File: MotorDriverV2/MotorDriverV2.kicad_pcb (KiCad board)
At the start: 2 copper layers, 9 parts, among them IC1 TC78H620FNG, IC2 ESP32-C3FH4X, J1 Power, J2 Input, J3 Out_A, J4 Out_B

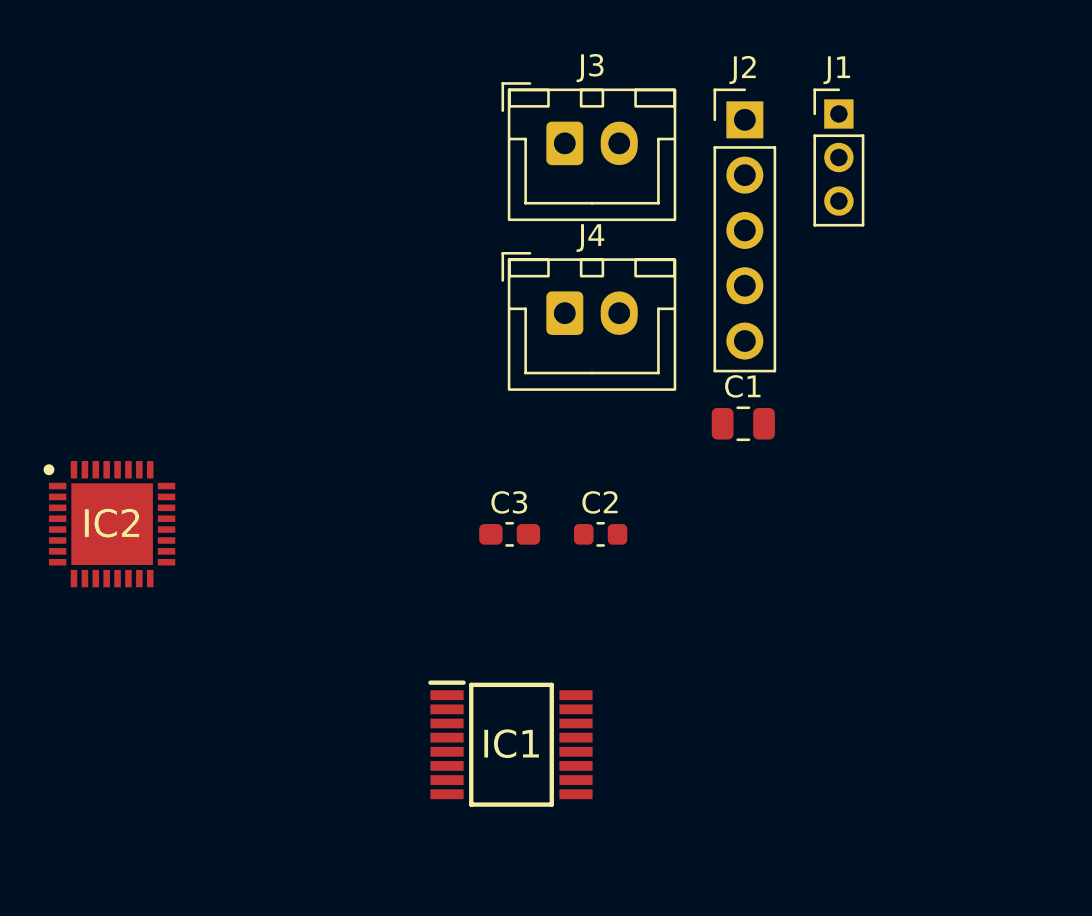
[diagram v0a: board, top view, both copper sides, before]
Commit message: UPDATE: Added symbols, fotprints and datasheets for components
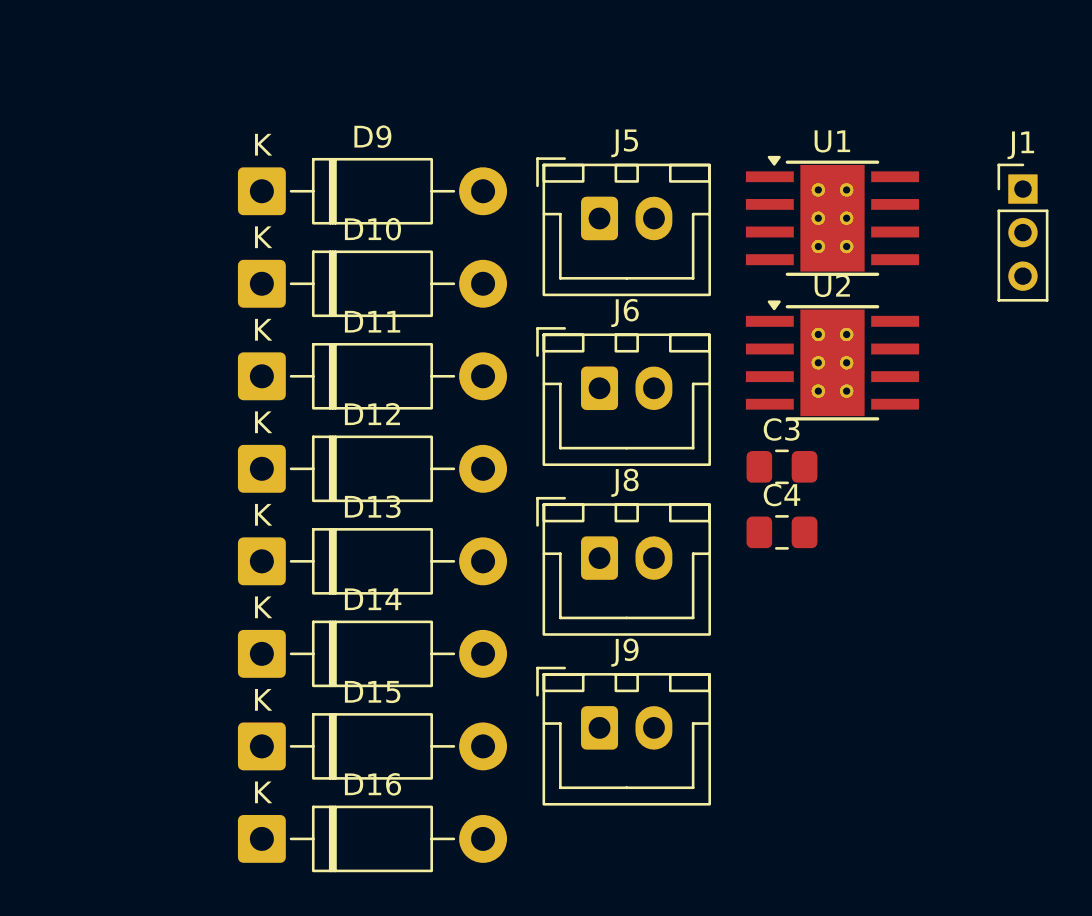
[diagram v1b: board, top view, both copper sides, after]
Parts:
- removed C1: 100uF, Capacitor_SMD:C_0805_2012Metric
- removed C2: C, Capacitor_SMD:C_0603_1608Metric
- removed IC1: TC78H620FNG, TC78H620FNG:SOP65P640X160-16N
- removed IC2: ESP32-C3FH4X, ESP32-C3FH4X:QFN50P500X500X90-33N-D
- removed J2: Input, Connector_PinHeader_2.54mm:PinHeader_1x05_P2.54mm_Vertical
- removed J3: Out_A, Connector_JST:JST_XH_B2B-XH-A_1x02_P2.50mm_Vertical
- removed J4: Out_B, Connector_JST:JST_XH_B2B-XH-A_1x02_P2.50mm_Vertical
- added C4: 100uF, Capacitor_SMD:C_0805_2012Metric_Pad1.18x1.45mm_HandSolder, F.Cu at (137.7, 82.5)
- added D10: 1N4001, Diode_THT:D_DO-41_SOD81_P10.16mm_Horizontal, F.Cu at (113.8, 71.0)
- added D11: 1N4001, Diode_THT:D_DO-41_SOD81_P10.16mm_Horizontal, F.Cu at (113.8, 75.3)
- added D12: 1N4001, Diode_THT:D_DO-41_SOD81_P10.16mm_Horizontal, F.Cu at (113.8, 79.5)
- added D13: 1N4001, Diode_THT:D_DO-41_SOD81_P10.16mm_Horizontal, F.Cu at (113.8, 83.8)
- added D14: 1N4001, Diode_THT:D_DO-41_SOD81_P10.16mm_Horizontal, F.Cu at (113.8, 88.0)
- added D15: 1N4001, Diode_THT:D_DO-41_SOD81_P10.16mm_Horizontal, F.Cu at (113.8, 92.3)
- added D16: 1N4001, Diode_THT:D_DO-41_SOD81_P10.16mm_Horizontal, F.Cu at (113.8, 96.5)
- added D9: 1N4001, Diode_THT:D_DO-41_SOD81_P10.16mm_Horizontal, F.Cu at (113.8, 66.8)
- added J5: Out_A, Connector_JST:JST_XH_B2B-XH-A_1x02_P2.50mm_Vertical, F.Cu at (129.4, 68.0)
- added J6: Out_B, Connector_JST:JST_XH_B2B-XH-A_1x02_P2.50mm_Vertical, F.Cu at (129.4, 75.8)
- added J8: Out_A, Connector_JST:JST_XH_B2B-XH-A_1x02_P2.50mm_Vertical, F.Cu at (129.4, 83.6)
- added J9: Out_B, Connector_JST:JST_XH_B2B-XH-A_1x02_P2.50mm_Vertical, F.Cu at (129.4, 91.4)
- added U1: DRV8871DDA, Package_SO:Texas_HTSOP-8-1EP_3.9x4.9mm_P1.27mm_EP2.95x4.9mm_Mask2.4x3.1mm_ThermalVias, F.Cu at (140.1, 68.0)
- added U2: DRV8871DDA, Package_SO:Texas_HTSOP-8-1EP_3.9x4.9mm_P1.27mm_EP2.95x4.9mm_Mask2.4x3.1mm_ThermalVias, F.Cu at (140.1, 74.7)
- C3: value C -> 100uF; footprint Capacitor_SMD:C_0603_1608Metric_Pad1.08x0.95mm_HandSolder -> Capacitor_SMD:C_0805_2012Metric_Pad1.18x1.45mm_HandSolder
- moved C3 12.9 mm to (137.7, 79.5)
- moved J1 9.13 mm to (148.8, 66.7)
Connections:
- C3 pad 1: unconnected-(C3-Pad1) -> +7.4V
- C3 pad 2: unconnected-(C3-Pad2) -> GND

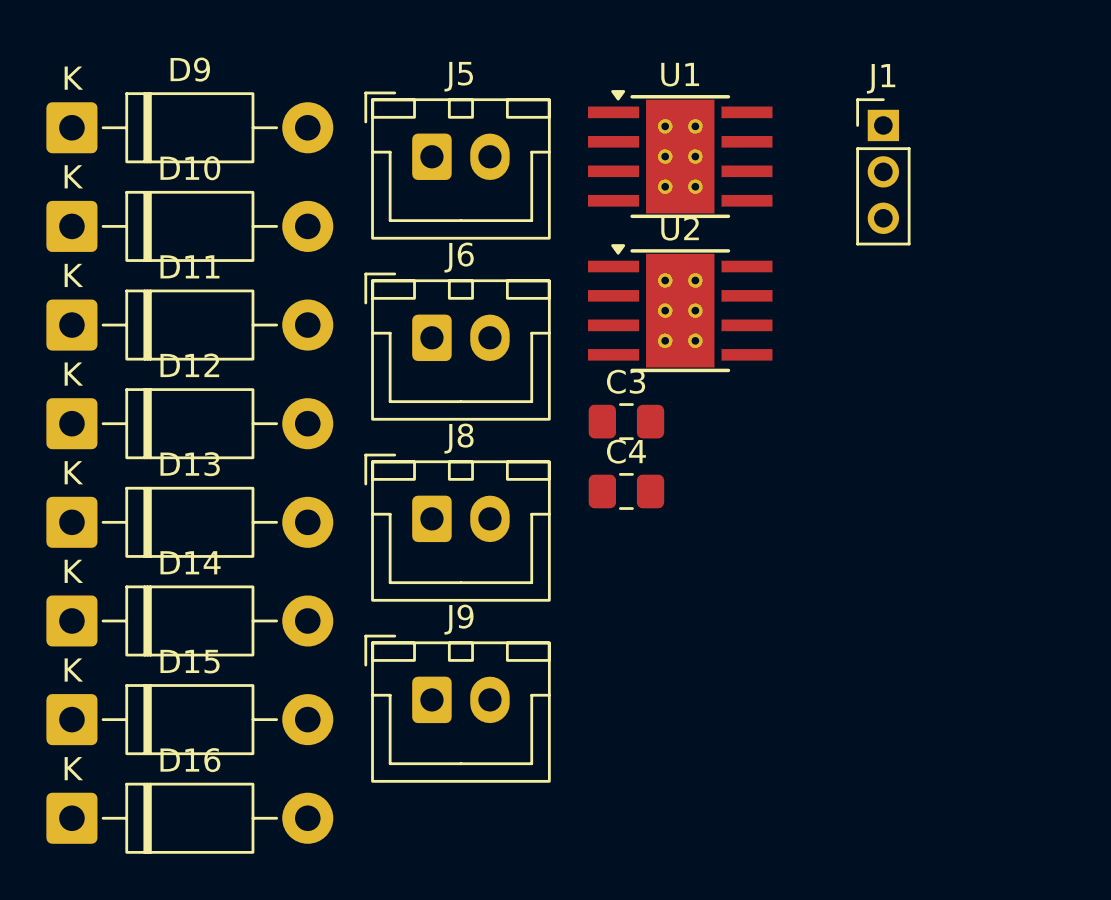
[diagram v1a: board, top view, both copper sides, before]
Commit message: UPDATE: Added symbols, fotprints and datasheets for components
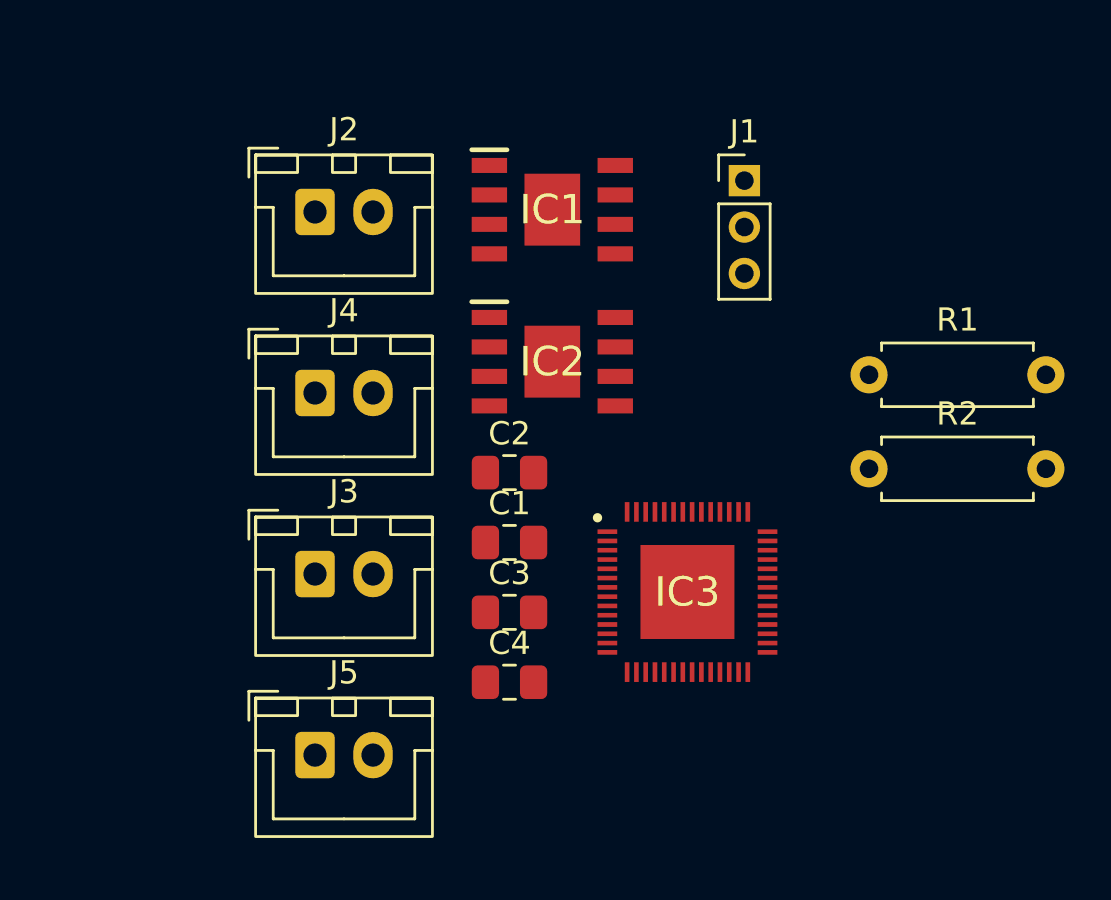
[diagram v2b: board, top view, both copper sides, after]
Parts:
- removed D10, D11, D12, D13, D14, D15, D16, D9: 1N4001, Diode_THT:D_DO-41_SOD81_P10.16mm_Horizontal
- removed J6, J9: Out_B, Connector_JST:JST_XH_B2B-XH-A_1x02_P2.50mm_Vertical
- removed J8: Out_A, Connector_JST:JST_XH_B2B-XH-A_1x02_P2.50mm_Vertical
- removed U1, U2: DRV8871DDA, Package_SO:Texas_HTSOP-8-1EP_3.9x4.9mm_P1.27mm_EP2.95x4.9mm_Mask2.4x3.1mm_ThermalVias
- added C1: 0.1uF, Capacitor_SMD:C_0805_2012Metric_Pad1.18x1.45mm_HandSolder, F.Cu at (132.7, 84.7)
- added C2: 47uF, Capacitor_SMD:C_0805_2012Metric_Pad1.18x1.45mm_HandSolder, F.Cu at (132.7, 81.6)
- added IC1: DRV8871DDARQ1, DRV8871DDARQ1:SOIC127P600X170-9N, F.Cu at (134.5, 70.3)
- added IC2: DRV8871DDARQ1, DRV8871DDARQ1:SOIC127P600X170-9N, F.Cu at (134.5, 76.9)
- added IC3: ESP32-S2FH4, ESP32-S2FH4:QFN40P700X700X90-57N-D, F.Cu at (140.4, 86.8)
- added J2: Out_A, Connector_JST:JST_XH_B2B-XH-A_1x02_P2.50mm_Vertical, F.Cu at (124.3, 70.4)
- added J3: Out_A, Connector_JST:JST_XH_B2B-XH-A_1x02_P2.50mm_Vertical, F.Cu at (124.3, 86.0)
- added J4: Out_B, Connector_JST:JST_XH_B2B-XH-A_1x02_P2.50mm_Vertical, F.Cu at (124.3, 78.2)
- added R1: 14.8K, Resistor_THT:R_Axial_DIN0207_L6.3mm_D2.5mm_P7.62mm_Horizontal, F.Cu at (148.2, 77.4)
- added R2: 14.8K, Resistor_THT:R_Axial_DIN0207_L6.3mm_D2.5mm_P7.62mm_Horizontal, F.Cu at (148.2, 81.5)
- C3: value 100uF -> 0.1uF
- C4: value 100uF -> 47uF
- J5: value Out_A -> Out_B
- moved J5 26.3 mm to (124.3, 93.8)
- moved C3 9.64 mm to (132.7, 87.7)
- moved C4 9.64 mm to (132.7, 90.7)
- moved J1 6.44 mm to (142.8, 69.1)
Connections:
- J5 pad 1: In1_2 -> Out2_1
- J5 pad 2: In1_1 -> Out2_2

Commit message: UPDATE: Schematic
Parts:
- removed C3: 0.1uF, Capacitor_SMD:C_0805_2012Metric_Pad1.18x1.45mm_HandSolder
- removed C4: 47uF, Capacitor_SMD:C_0805_2012Metric_Pad1.18x1.45mm_HandSolder
- removed J5: Out_B, Connector_JST:JST_XH_B2B-XH-A_1x02_P2.50mm_Vertical
- added C6: 0.1uF, Capacitor_SMD:C_0805_2012Metric_Pad1.18x1.45mm_HandSolder, F.Cu at (113.1, 61.3)
- added C7: 47uF, Capacitor_SMD:C_0805_2012Metric_Pad1.18x1.45mm_HandSolder, F.Cu at (113.1, 64.3)
- added D1: LED, LED_SMD:LED_0805_2012Metric_Pad1.15x1.40mm_HandSolder, F.Cu at (89.5, 65.1)
- added PS1: LM1117IMPX-3.3_NOPB, LM1117IMPX-3.3:SOT230P700X180-4N, F.Cu at (86.7, 59.4)
- added R3: 10k, Resistor_THT:R_Axial_DIN0207_L6.3mm_D2.5mm_P7.62mm_Horizontal, F.Cu at (83.5, 41.1)
- added R4: 5k1, Resistor_THT:R_Axial_DIN0207_L6.3mm_D2.5mm_P7.62mm_Horizontal, F.Cu at (83.5, 45.2)
- added R5: 5k1, Resistor_THT:R_Axial_DIN0207_L6.3mm_D2.5mm_P7.62mm_Horizontal, F.Cu at (83.5, 49.2)
- added R6: 5k1, Resistor_THT:R_Axial_DIN0207_L6.3mm_D2.5mm_P7.62mm_Horizontal, F.Cu at (83.5, 53.3)
- added U1: USBLC6-2SC6, Package_TO_SOT_SMD:SOT-23-6, F.Cu at (84.5, 65.9)
- IC3: value ESP32-S2FH4 -> ESP32-S3-WROOM-1U-N4; footprint ESP32-S2FH4:QFN40P700X700X90-57N-D -> ESP32-S3-WROOM-1U-N4:ESP32S3WROOM1UN4
- J3: value Out_A -> Conn_01x10_Pin; footprint Connector_JST:JST_XH_B2B-XH-A_1x02_P2.50mm_Vertical -> Connector_PinHeader_2.54mm:PinHeader_1x10_P2.54mm_Vertical
- moved R1 78.5 mm to (83.5, 33.0)
- moved R2 78.5 mm to (83.5, 37.1)
- moved J3 69.1 mm to (79.6, 33.3)
- moved J1 64.0 mm to (79.4, 60.5)
- moved IC3 57.6 mm to (103.7, 42.4)
- moved C1 35.3 mm to (113.1, 55.3)
- moved J2 31.1 mm to (96.2, 57.2)
- moved J4 31.1 mm to (96.2, 65.0)
- moved IC1 31.1 mm to (106.4, 57.1)
- moved IC2 31.1 mm to (106.4, 63.6)
- moved C2 30.5 mm to (113.1, 58.3)
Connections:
- IC3 pad 1: unconnected-(IC3-VDDA_1-Pad1) -> GND
- IC3 pad 12: unconnected-(IC3-GPIO7-Pad12) -> /IO_08
- IC3 pad 13: unconnected-(IC3-GPIO8-Pad13) -> /IO_19
- IC3 pad 14: unconnected-(IC3-GPIO9-Pad14) -> /IO_20
- IC3 pad 15: unconnected-(IC3-GPIO10-Pad15) -> /IO_03
- IC3 pad 16: unconnected-(IC3-GPIO11-Pad16) -> /IO_46
- IC3 pad 17: unconnected-(IC3-GPIO12-Pad17) -> /IO_09
- IC3 pad 18: unconnected-(IC3-GPIO13-Pad18) -> /IO_10
- IC3 pad 19: unconnected-(IC3-GPIO14-Pad19) -> /IO_11
- IC3 pad 2: unconnected-(IC3-LNA_IN-Pad2) -> +3V3
- IC3 pad 27: unconnected-(IC3-VDD3P3_RTC_IO-Pad27) -> /BOOT
- IC3 pad 3: unconnected-(IC3-VDD3P3_1-Pad3) -> /EN
- IC3 pad 4: unconnected-(IC3-VDD3P3_2-Pad4) -> In2_1
- IC3 pad 40: unconnected-(IC3-GPIO36-Pad40) -> GND
- IC3 pad 41: unconnected-(IC3-GPIO37-Pad41) -> GND
- IC3 pad 42: unconnected-(IC3-GPIO38-Pad42) -> GND
- IC3 pad 43: unconnected-(IC3-MTCK-Pad43) -> GND
- IC3 pad 44: unconnected-(IC3-MTD0-Pad44) -> GND
- IC3 pad 45: unconnected-(IC3-VDD3P3_CPU-Pad45) -> GND
- IC3 pad 46: unconnected-(IC3-MTDI-Pad46) -> GND
- IC3 pad 47: unconnected-(IC3-MTMS-Pad47) -> GND
- IC3 pad 48: unconnected-(IC3-U0TXD-Pad48) -> GND
- IC3 pad 49: unconnected-(IC3-U0RXD-Pad49) -> GND
- IC3 pad 5: unconnected-(IC3-GPIO0-Pad5) -> In2_2
- IC3 pad 6: unconnected-(IC3-GPIO1-Pad6) -> In1_2
- IC3 pad 7: unconnected-(IC3-GPIO2-Pad7) -> In1_1
- J2 pad 1: In1_1 -> Out1_1
- J2 pad 2: In1_2 -> Out1_2
- J3 pad 1: Out1_1 -> GND
- J3 pad 2: Out1_2 -> +3V3
- J4 pad 1: In2_2 -> Out2_1
- J4 pad 2: In2_1 -> Out2_2
